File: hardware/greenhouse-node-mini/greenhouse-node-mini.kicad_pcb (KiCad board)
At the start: 4 copper layers, 70 x 50 mm, 40 parts, among them J1 Molex_KK_396_1x2, J2 JST_XH_2.54mm_1x2, J4 Molex_KK_396_1x2, J5 JST_XH_2.54mm_1x4, J6 PinHeader_1x04_P2.54mm, J7 PinHeader_1x04_P2.54mm, Q1 A42, U1 ATtiny84A-P, U2 L7805, U3 PCF8574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

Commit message: Set IO address to 0x20/0x65/0x64
According to internet, 0x20
According to datasheet, 0x65/0x64
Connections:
- U3 pad 1: unconnected-(U3-Pad1) -> GND
- U3 pad 2: unconnected-(U3-Pad2) -> GND
- U3 pad 3: unconnected-(U3-Pad3) -> GND

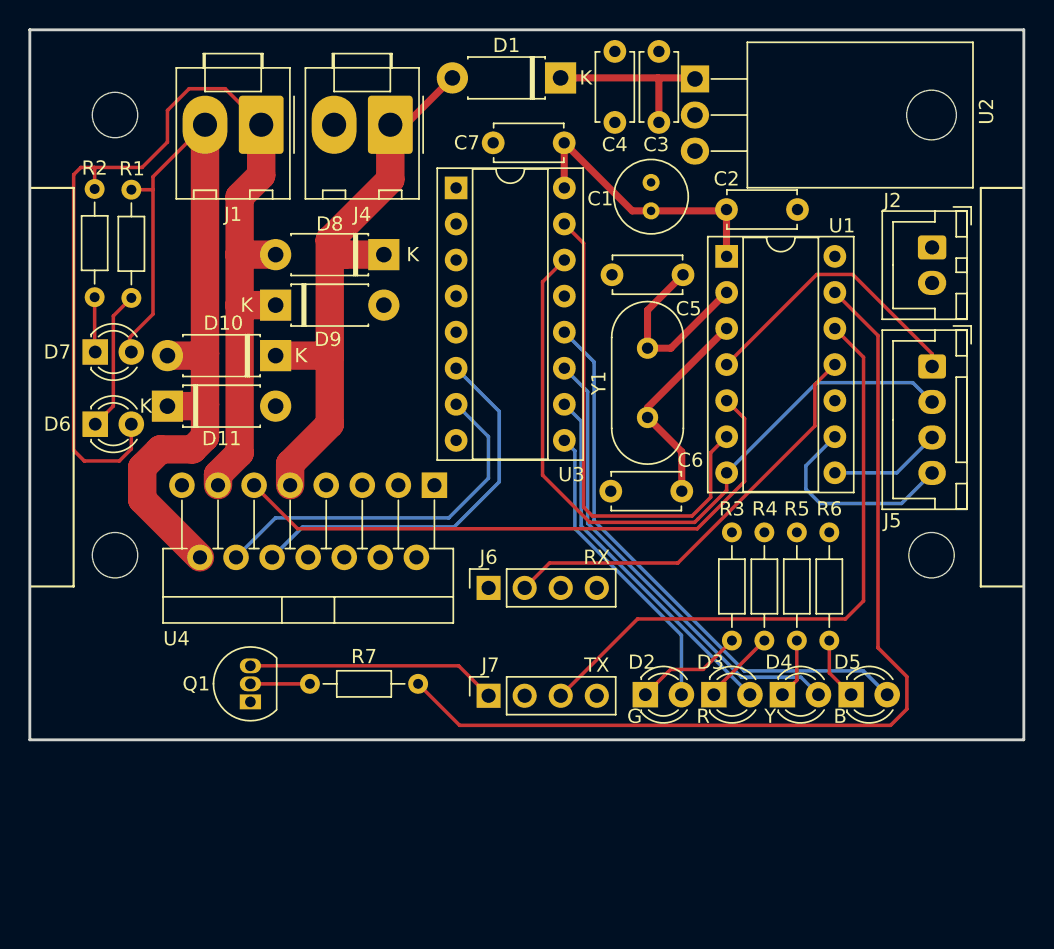
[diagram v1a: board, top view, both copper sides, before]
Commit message: Add I2C pull-ups
Also reorganised schematic
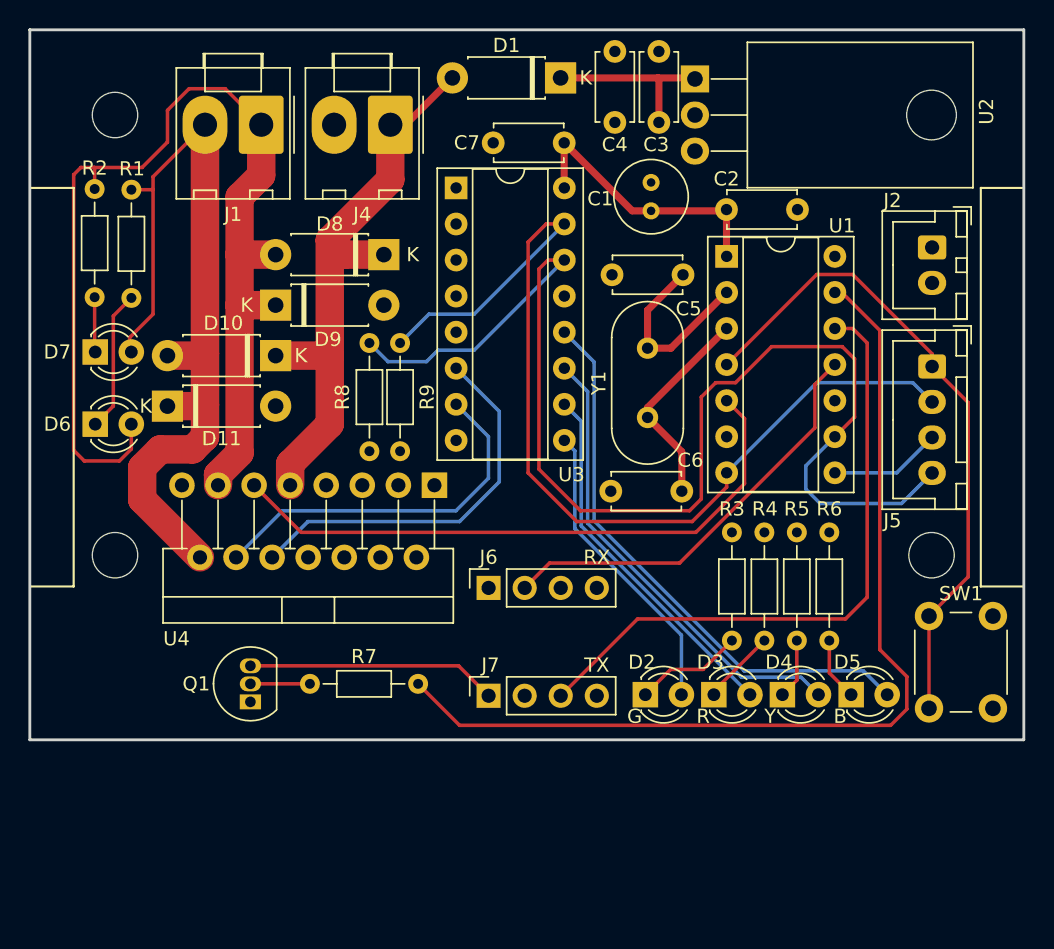
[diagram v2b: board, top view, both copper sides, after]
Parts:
- added R8: 10k, Resistor_THT:R_Axial_DIN0204_L3.6mm_D1.6mm_P7.62mm_Horizontal, F.Cu at (89.9, 66.7)
- added R9: 10k, Resistor_THT:R_Axial_DIN0204_L3.6mm_D1.6mm_P7.62mm_Horizontal, F.Cu at (92.1, 66.7)
- added SW1: SW_Push, Button_Switch_THT:SW_PUSH_6mm, F.Cu at (129.3, 84.8)
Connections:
- U1 pad 6: Net-(U1-Pad6) -> unconnected-(U1-Pad6)
- U3 pad 14: /PGM_A -> /PGM_C
- U3 pad 15: Net-(U1-Pad6) -> /PGM_A
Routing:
- net /PGM_C: track 14.7 -> 87.0 mm
- net Net-(U1-Pad6): track 35.0 -> 0.00 mm
- net /Reset: track 20.3 -> 46.6 mm
- net /PGM_A: track 50.0 -> 69.4 mm
- net /RAD_TX: track 44.1 -> 45.1 mm

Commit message: Change LEDs to current sink (PCB WIP)
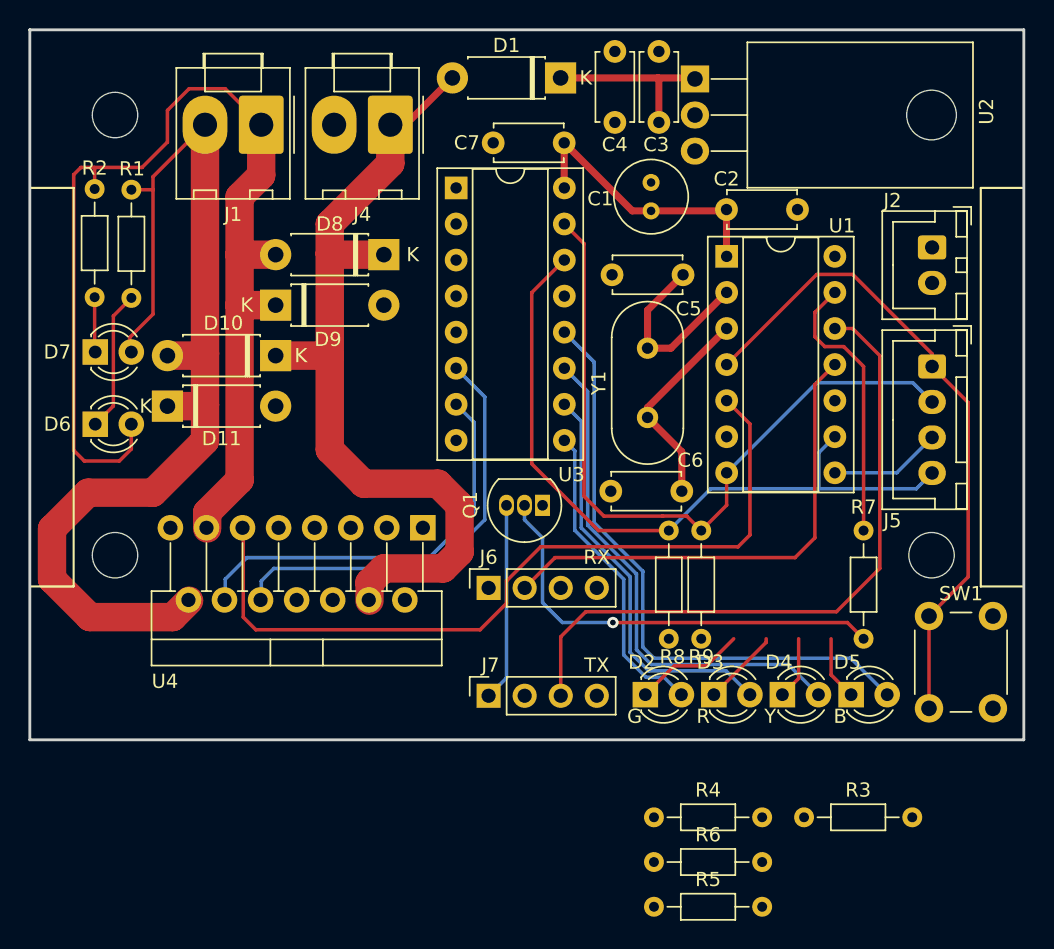
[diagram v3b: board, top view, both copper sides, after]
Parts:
- moved R7 39.1 mm to (124.7, 79.9), turned to 90 degrees
- moved R5 28.2 mm to (110.0, 98.8), turned to 0 degrees
- moved R6 26.3 mm to (110.0, 95.6), turned to 0 degrees
- moved R9 25.0 mm to (113.3, 79.9)
- moved R8 24.9 mm to (111.0, 79.9)
- moved Q1 24.8 mm to (102.1, 70.5), turned to 180 degrees
- moved R4 21.5 mm to (110.0, 92.5), turned to 0 degrees
- moved R3 20.7 mm to (120.5, 92.5), turned to 0 degrees
- moved U4 3.11 mm to (93.7, 72.1)
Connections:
- D2 pad 2: /LED_G -> +5V
- D3 pad 2: /LED_R -> +5V
- D4 pad 2: /LED_Y -> +5V
- D5 pad 2: /LED_B -> +5V
- R3 pad 1: GND -> /LED_G
- R4 pad 1: GND -> /LED_R
- R5 pad 1: GND -> /LED_Y
- R6 pad 1: GND -> /LED_B
- U4 pad 4: +5V -> +10V
- U4 pad 9: +10V -> +5V
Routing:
- net +5V: track 19.8 -> 150.0 mm
- net /RAD_TX_EN: track 67.8 -> 19.6 mm
- net /LED_B: track 39.9 -> 0.00 mm
- net /PGM_C: track 87.0 -> 51.3 mm
- net /LED_Y: track 32.9 -> 0.00 mm
- net Net-(Q1-Pad2): track 4.19 -> 30.7 mm, vias 0 -> 1
- net /LED_R: track 25.9 -> 0.00 mm
- net /LED_G: track 21.3 -> 0.00 mm
- net +10V: track 41.0 -> 59.5 mm
- net /PGM_A: track 69.4 -> 51.5 mm
- net /M_OUT2: track 60.4 -> 75.5 mm
- net /M_EN: track 43.7 -> 56.1 mm
- net /RAD_RX: track 30.1 -> 34.7 mm
- net Net-(J7-Pad1): track 17.6 -> 13.9 mm
- net /M_OUT1: track 77.2 -> 80.6 mm
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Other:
- board text added: "Heatsink"

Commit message: Reorganised node mini PCB
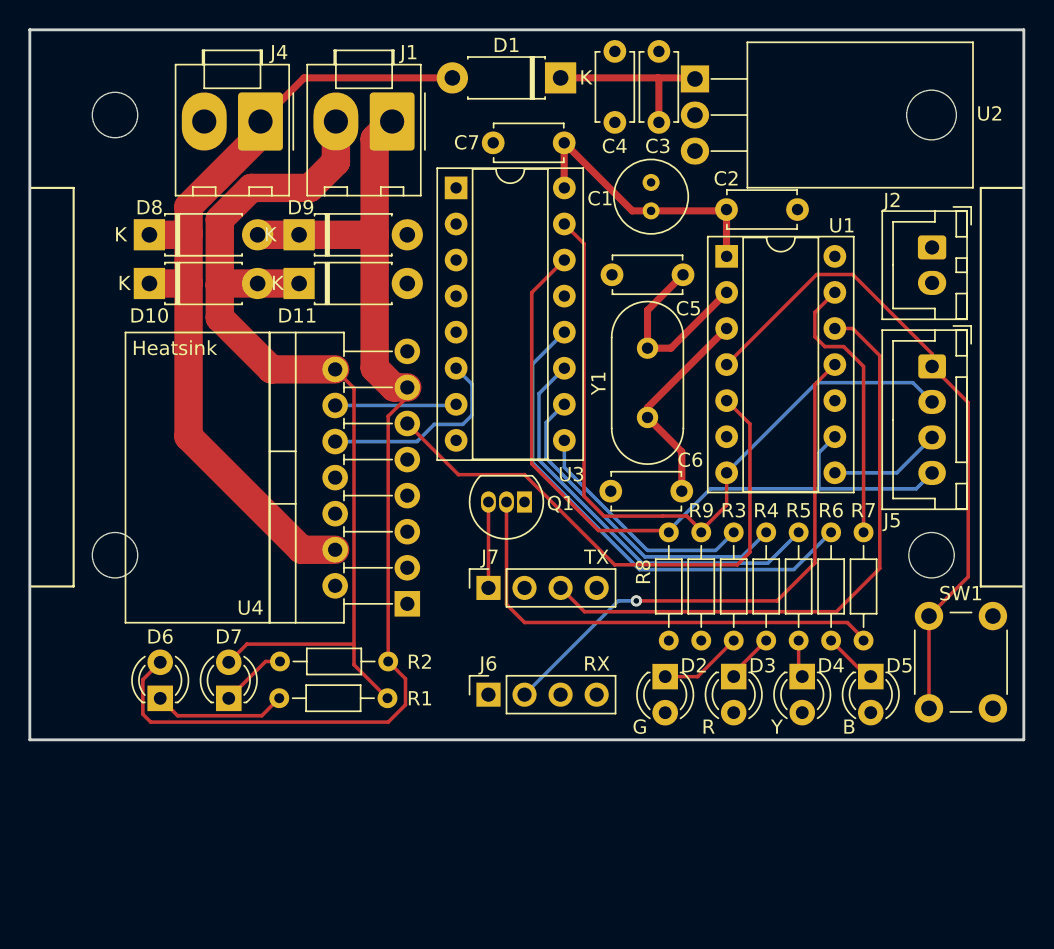
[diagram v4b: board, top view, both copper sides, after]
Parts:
- moved R1 40.1 mm to (91.2, 84.1), turned to 180 degrees
- moved R2 39.2 mm to (91.2, 81.5), turned to 180 degrees
- moved R5 28.3 mm to (120.1, 72.4), turned to -90 degrees
- moved R6 26.4 mm to (122.4, 72.4), turned to -90 degrees
- moved D7 26.1 mm to (80.0, 84.1), turned to 90 degrees
- moved R4 21.6 mm to (117.9, 72.4), turned to -90 degrees
- moved R3 20.7 mm to (115.6, 72.4), turned to -90 degrees
- moved D6 19.8 mm to (75.2, 84.1), turned to 90 degrees
- moved D8 16.6 mm to (74.4, 51.4), turned to 0 degrees
- moved D11 12.7 mm to (85.0, 54.9)
- moved D10 10.2 mm to (74.4, 54.9), turned to 0 degrees
- moved J1 9.22 mm to (91.5, 43.5)
- moved J4 9.15 mm to (82.2, 43.5)
- moved J7 7.60 mm to (98.3, 76.3)
- moved J6 7.52 mm to (98.3, 83.8)
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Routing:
- net +5V: track 150.0 -> 19.8 mm
- net /LED_B: track 0.00 -> 35.3 mm
- net /LED_Y: track 0.00 -> 29.4 mm
- net /LED_R: track 0.00 -> 23.4 mm
- net /M_IN2: track 29.1 -> 8.44 mm
- net /LED_G: track 0.00 -> 16.8 mm
- net /M_IN1: track 30.4 -> 14.2 mm
- net /M_EN: track 56.1 -> 40.0 mm
- net Net-(J7-Pad1): track 13.9 -> 6.05 mm
- net /M_OUT2: track 75.5 -> 68.9 mm
- net /M_OUT1: track 80.6 -> 75.1 mm
- net /RAD_TX: track 47.6 -> 43.4 mm
- net /RAD_RX: track 34.7 -> 38.8 mm, vias 0 -> 1
- net Net-(Q1-Pad2): track 30.7 -> 33.4 mm, vias 1 -> 0
- net Net-(D3-Pad1): track 5.46 -> 3.23 mm
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
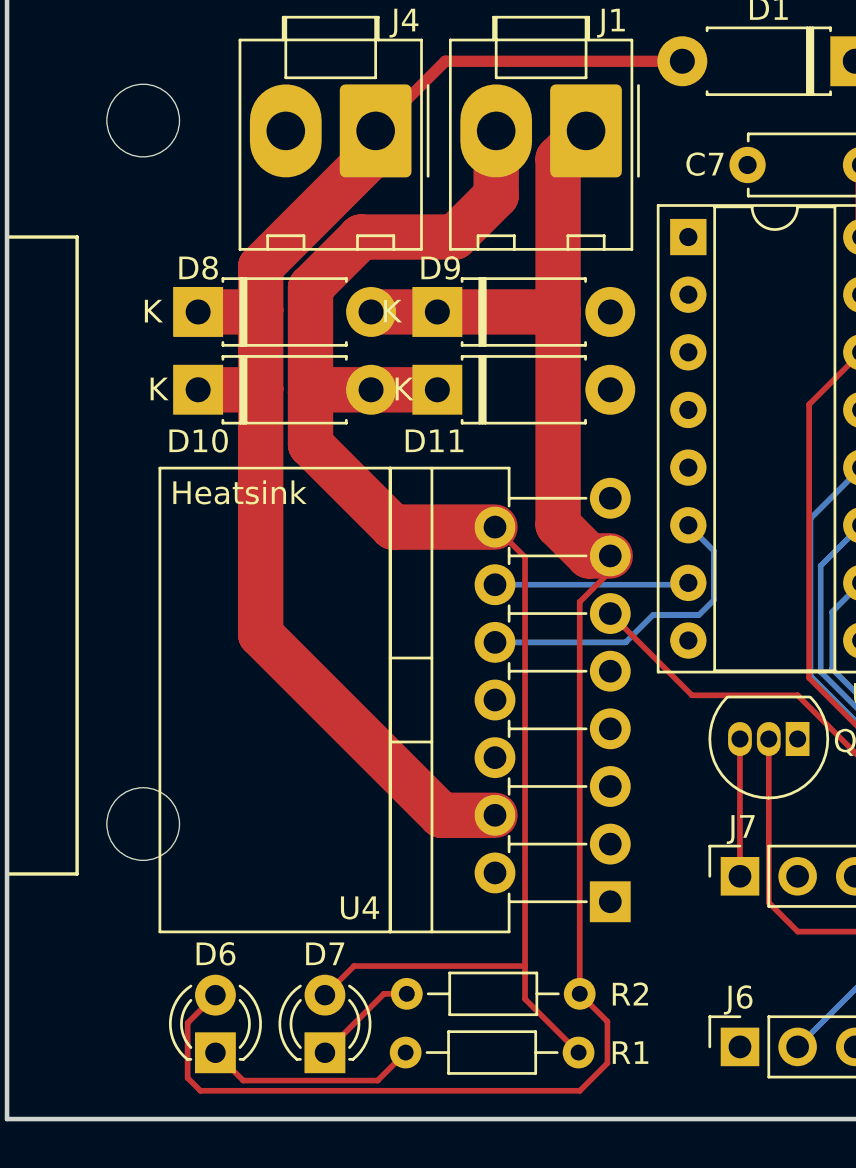
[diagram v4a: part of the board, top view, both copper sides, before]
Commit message: Tweak traces and silkscreen
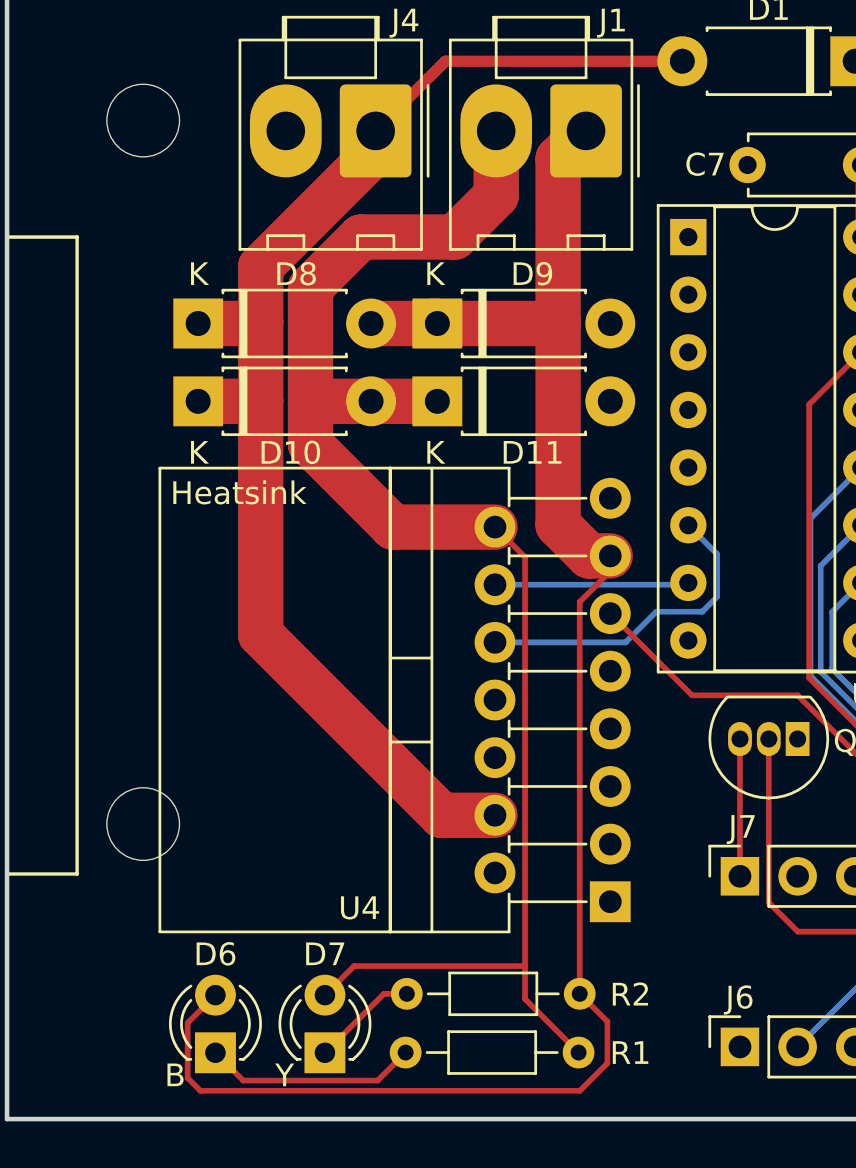
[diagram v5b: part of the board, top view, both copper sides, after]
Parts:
- moved D10 0.51 mm to (74.4, 55.4)
- moved D11 0.51 mm to (85.0, 55.4)
- moved D8 0.51 mm to (74.4, 51.9)
- moved D9 0.51 mm to (85.0, 51.9)

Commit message: More track tweaking
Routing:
- net +10V: track 57.3 -> 52.4 mm
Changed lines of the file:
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@@
   (segment (start 123.317 59.309) (end 124.714 60.706) (width 0.25) (layer "F.Cu") (net 4))
   (segment (start 121.285 56.901) (end 121.285 58.6105) (width 0.25) (layer "F.Cu") (net 4))
-  (segment (start 77.17548 51.85652) (end 77.17548 55.33148) (width 2) (layer "F.Cu") (net 5))
-  (segment (start 77.13496 55.372) (end 77.17548 55.33148) (width 2) (layer "F.Cu") (net 5))
-  (segment (start 77.17548 49.444429) (end 77.17548 51.85652) (width 2) (layer "F.Cu") (net 5))
-  (segment (start 77.17548 65.64388) (end 85.1458 73.6142) (width 2) (layer "F.Cu") (net 5))
-  (segment (start 74.422 51.943) (end 77.089 51.943) (width 2) (layer "F.Cu") (net 5))
+  (segment (start 82.244 44.375909) (end 76.454 50.165909) (width 2) (layer "F.Cu") (net 5))
   (segment (start 85.1458 73.6142) (end 87.503 73.6142) (width 2) (layer "F.Cu") (net 5))
   (segment (start 95.758 40.386) (end 85.314 40.386) (width 0.5) (layer "F.Cu") (net 5))
-  (segment (start 77.089 51.943) (end 77.17548 51.85652) (width 2) (layer "F.Cu") (net 5))
+  (segment (start 76.454 64.9224) (end 85.1458 73.6142) (width 2) (layer "F.Cu") (net 5))
+  (segment (start 76.454 50.165909) (end 76.454 64.9224) (width 2) (layer "F.Cu") (net 5))
   (segment (start 85.314 40.386) (end 82.244 43.456) (width 0.5) (layer "F.Cu") (net 5))
-  (segment (start 77.17548 55.33148) (end 77.17548 65.64388) (width 2) (layer "F.Cu") (net 5))
-  (segment (start 82.244 44.375909) (end 77.17548 49.444429) (width 2) (layer "F.Cu") (net 5))
-  (segment (start 74.422 55.372) (end 77.13496 55.372) (width 2) (layer "F.Cu") (net 5))
   (segment (start 113.284 72.263) (end 112.259489 71.238489) (width 0.25) (layer "F.Cu") (net 6))
   (segment (start 112.259489 71.238489) (end 110.573633 71.238489) (width 0.25) (layer "F.Cu") (net 6))
@@
   (segment (start 75.184 81.539) (end 73.959489 82.763511) (width 0.25) (layer "F.Cu") (net 19))
   (segment (start 91.6482 62.1842) (end 90.283489 60.819489) (width 2) (layer "F.Cu") (net 19))
+  (segment (start 79.375 50.927) (end 79.375 55.372) (width 2) (layer "F.Cu") (net 20))
   (segment (start 83.0122 60.9142) (end 87.503 60.9142) (width 2) (layer "F.Cu") (net 20))
+  (segment (start 87.555 46.303) (end 84.963 48.895) (width 2) (layer "F.Cu") (net 20))
+  (segment (start 88.82752 81.71052) (end 88.82752 62.23872) (width 0.25) (layer "F.Cu") (net 20))
+  (segment (start 80.01 81.539) (end 81.29 80.259) (width 0.25) (layer "F.Cu") (net 20))
   (segment (start 87.555 43.456) (end 87.555 46.303) (width 2) (layer "F.Cu") (net 20))
-  (segment (start 81.5975 48.133) (end 79.375 50.3555) (width 2) (layer "F.Cu") (net 20))
-  (segment (start 88.82752 81.71052) (end 88.82752 62.23872) (width 0.25) (layer "F.Cu") (net 20))
-  (segment (start 79.375 57.277) (end 83.0122 60.9142) (width 2) (layer "F.Cu") (net 20))
-  (segment (start 80.01 81.539) (end 81.29 80.259) (width 0.25) (layer "F.Cu") (net 20))
-  (segment (start 87.555 46.303) (end 85.725 48.133) (width 2) (layer "F.Cu") (net 20))
-  (segment (start 79.375 50.3555) (end 79.375 55.499) (width 2) (layer "F.Cu") (net 20))
+  (segment (start 82.042 55.372) (end 79.375 55.372) (width 2) (layer "F.Cu") (net 20))
   (segment (start 88.82752 62.23872) (end 87.503 60.9142) (width 0.25) (layer "F.Cu") (net 20))
+  (segment (start 84.963 48.895) (end 81.407 48.895) (width 2) (layer "F.Cu") (net 20))
   (segment (start 91.186 84.069) (end 88.82752 81.71052) (width 0.25) (layer "F.Cu") (net 20))
   (segment (start 84.963 55.372) (end 82.042 55.372) (width 2) (layer "F.Cu") (net 20))
-  (segment (start 85.725 48.133) (end 81.5975 48.133) (width 2) (layer "F.Cu") (net 20))
-  (segment (start 79.375 55.499) (end 79.375 57.277) (width 2) (layer "F.Cu") (net 20))
-  (segment (start 82.042 55.372) (end 79.502 55.372) (width 2) (layer "F.Cu") (net 20))
+  (segment (start 79.375 57.277) (end 83.0122 60.9142) (width 2) (layer "F.Cu") (net 20))
   (segment (start 81.29 80.259) (end 88.82752 80.259) (width 0.25) (layer "F.Cu") (net 20))
-  (segment (start 79.502 55.372) (end 79.375 55.499) (width 2) (layer "F.Cu") (net 20))
+  (segment (start 81.407 48.895) (end 79.375 50.927) (width 2) (layer "F.Cu") (net 20))
+  (segment (start 79.375 55.372) (end 79.375 57.277) (width 2) (layer "F.Cu") (net 20))
   (segment (start 121.417 54.229) (end 115.072 60.574) (width 0.25) (layer "F.Cu") (net 23))
   (segment (start 123.952 54.229) (end 121.417 54.229) (width 0.25) (layer "F.Cu") (net 23))
